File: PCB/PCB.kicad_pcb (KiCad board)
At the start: 2 copper layers, 121.6 x 80 mm, 113 parts, among them J1 AudioJack3, J2 Conn, J3 Screw_Terminal_01x02, J4 Screw_Terminal_01x02, J5 Screw_Terminal_01x02, J6 Screw_Terminal_01x02, Q1 Q_NPN_BCE, Q10 Q_NPN, Q11 Q_PNP_BCE, Q12 Q_NPN, Q13 Q_PNP, Q14 Q_PNP_BCE, Q15 Q_PNP_BCE, Q16 Q-NPN, Q17 Q-NPN, Q18 Q-NPN, Q19 Q-PNP, Q2 Q_PNP_BCE, Q20 Q-NPN, Q21 Q-PNP, Q22 Q-NPN, Q23 Q-PNP, Q24 Q-PNP, Q25 Q-NPN, Q26 Q-NPN, Q27 Q-PNP, Q28 Q-NPN, Q29 Q_PNP, Q3 Q_NPN_BCE, Q4 Q_PNP_BCE, Q5 Q_NPN_BCE, Q6 Q_PNP_BCE, Q7 Q_PNP_BCE, Q8 Q_NPN_BCE, Q9 Q_NPN_BCE

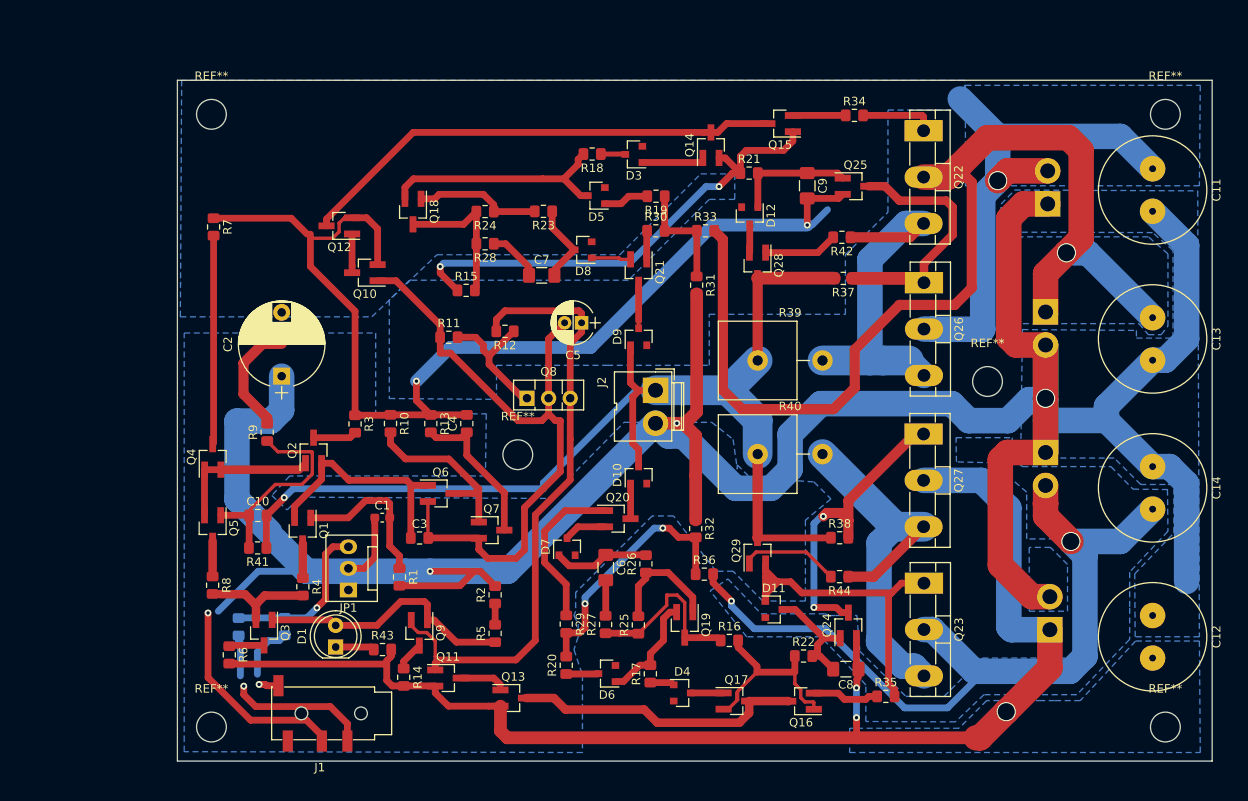
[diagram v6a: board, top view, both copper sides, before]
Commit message: Footprint actualizados. se agrando el pcb para los capacitores. Se agregaron algunos valores de componentes en el esquematico
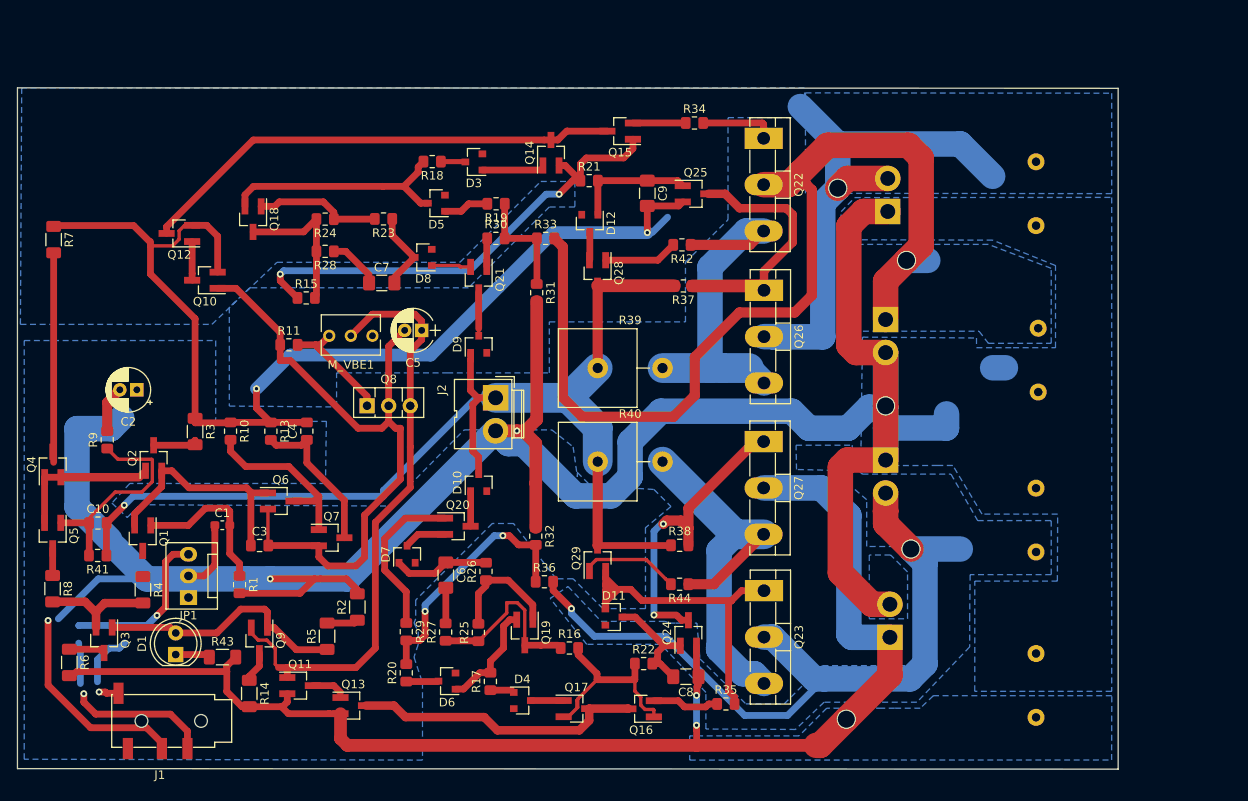
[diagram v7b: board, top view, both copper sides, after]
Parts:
- removed R12, R45, R46: R, Resistor_SMD:R_0805_2012Metric_Pad1.15x1.40mm_HandSolder
- removed REF** (x6): MountingHole_3.5mm, Mounting_Holes:MountingHole_3.5mm
- added M_VBE1: 5k, Potentiometer_THT:Potentiometer_Bourns_3266Y_Vertical, F.Cu at (174.2, 79.6)
- C11, C12, C13, C14: footprint Capacitor_THT:C_Radial_D12.5mm_H20.0mm_P5.00mm -> Capacitor_THT:C_Radial_D18.0mm_H35.5mm_P7.50mm; moved to B.Cu
- C2: value C -> 47u; footprint Capacitors_THT:CP_Radial_D10.0mm_P7.50mm -> Capacitor_THT:CP_Radial_D5.0mm_P2.00mm
- C3: value C -> 20p
- C4: value C -> 1u
- C5: value C -> 4.7u
- Q1, Q5, Q9: value Q_NPN_BCE -> MMBTA06
- Q2, Q4, Q6, Q7: value Q_PNP_BCE -> MMBTA56
- Q8: value Q_NPN_BCE -> MJE340
- R1: value R -> 20k
- R10: value R -> 1k
- R11: value R -> 2.2k
- R13: value R -> 10
- R14: value R -> 470; footprint Resistor_SMD:R_0805_2012Metric_Pad1.15x1.40mm_HandSolder -> Resistor_SMD:R_1206_3216Metric_Pad1.30x1.75mm_HandSolder
- R2, R5: value R -> 4.7k; footprint Resistor_SMD:R_0805_2012Metric_Pad1.15x1.40mm_HandSolder -> Resistor_SMD:R_1206_3216Metric_Pad1.30x1.75mm_HandSolder
- R3, R4, R7, R8: value R -> 22; footprint Resistor_SMD:R_0805_2012Metric_Pad1.15x1.40mm_HandSolder -> Resistor_SMD:R_1206_3216Metric_Pad1.30x1.75mm_HandSolder
- R43: value R -> TBD; footprint Resistor_SMD:R_0805_2012Metric_Pad1.15x1.40mm_HandSolder -> Resistor_SMD:R_1206_3216Metric_Pad1.30x1.75mm_HandSolder
- R6: value R -> 2.2k; footprint Resistor_SMD:R_0805_2012Metric_Pad1.15x1.40mm_HandSolder -> Resistor_SMD:R_1206_3216Metric_Pad1.30x1.75mm_HandSolder
- R9: value R -> 1.2k
- moved R5 19.7 mm to (174.0, 114.9)
- moved R7 18.9 mm to (141.9, 68.3)
- moved C6 18.8 mm to (187.9, 107.8)
- moved D11 18.8 mm to (207.7, 112.7)
- moved D8 18.8 mm to (185.3, 70.4)
- moved J2 18.8 mm to (193.8, 86.9)
- moved J3 18.8 mm to (239.9, 65.0)
- moved Q10 18.8 mm to (159.6, 73.1)
- moved Q12 18.8 mm to (156.6, 67.6)
- moved Q17 18.8 mm to (203.3, 123.4)
- moved Q18 18.8 mm to (165.3, 65.9)
- moved Q19 18.8 mm to (197.2, 114.5)
- moved Q20 18.8 mm to (189.4, 102.0)
- moved Q22 18.8 mm to (225.3, 56.4)
- moved Q23 18.8 mm to (225.3, 109.6)
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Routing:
- net GND: track 356.2 -> 303.2 mm
- net +15V: track 129.1 -> 118.3 mm
- net Net-(C2-Pad2): track 13.7 -> 5.47 mm
- net -15V: track 95.9 -> 90.6 mm
- net Net-(J1-PadS) (its old number): track 4.83 -> 0.00 mm
- net Net-(J1-PadS): track 19.5 -> 24.3 mm
- net Net-(Q1-Pad3): track 4.09 -> 0.04 mm
- net Net-(C5-Pad1): track 73.7 -> 71.1 mm
- net VEE: track 155.4 -> 157.4 mm
- net Net-(Q11-Pad3): track 5.60 -> 4.19 mm
- net Net-(R2-Pad1): track 2.48 -> 3.69 mm
- net Net-(Q5-Pad3): track 4.19 -> 3.19 mm
- net Net-(D1-Pad2): track 30.7 -> 29.8 mm
- net Net-(M_VBE1-Pad1): track 16.2 -> 15.6 mm
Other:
- board size 121.6 x 80 mm -> 129.3 x 80.1 mm

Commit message: More footprint changes. Added some modifications to the pcb
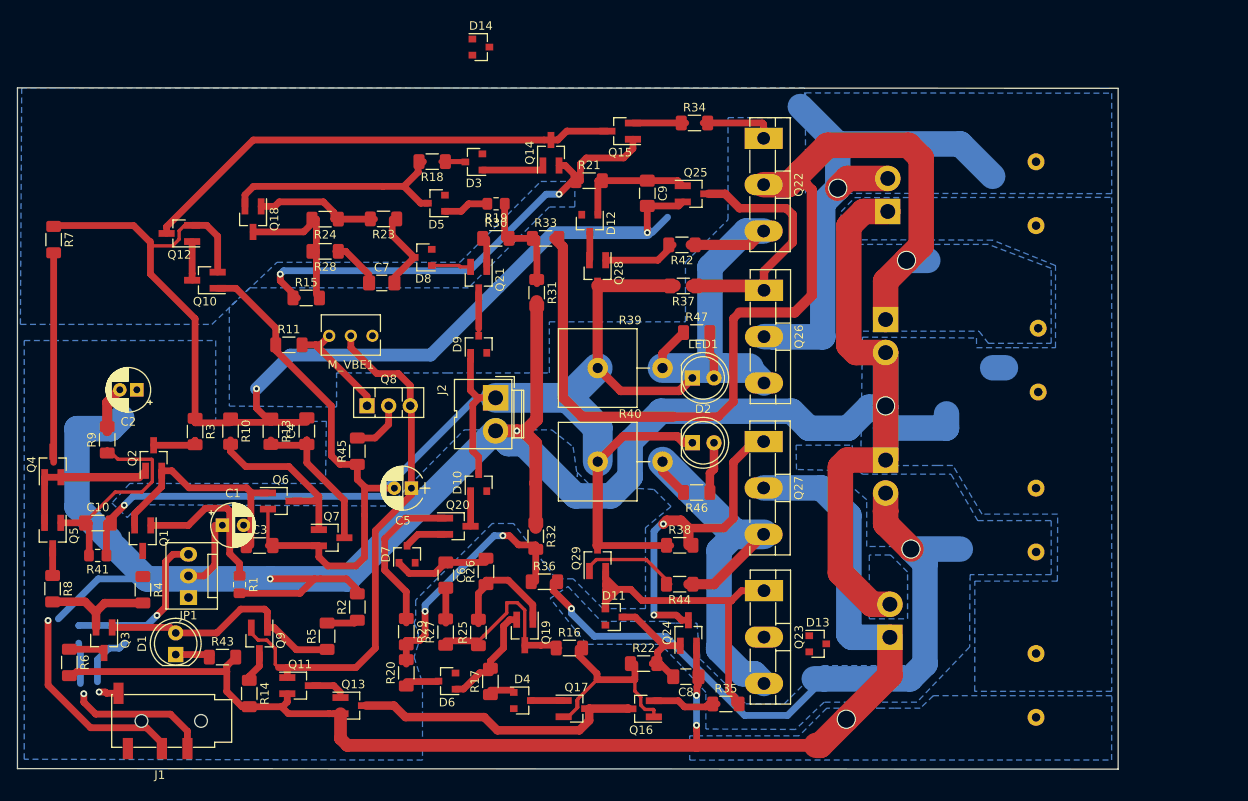
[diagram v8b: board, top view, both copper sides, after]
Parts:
- added D13: BAT54, Diode_SMD:D_SOT-23_ANK, F.Cu at (231.6, 115.8)
- added D14: BAT54, Diode_SMD:D_SOT-23_ANK, F.Cu at (192.1, 45.7)
- added D2: LED, LED_THT:LED_D5.0mm, F.Cu at (216.9, 92.2)
- added LED1: LED_ALT, LED_THT:LED_D5.0mm, F.Cu at (216.9, 84.6)
- added R45: 22, Resistor_SMD:R_1206_3216Metric_Pad1.30x1.75mm_HandSolder, F.Cu at (177.5, 93.2)
- added R46: TBD, Resistor_SMD:R_1206_3216Metric_Pad1.30x1.75mm_HandSolder, F.Cu at (217.4, 98.0)
- added R47: TBD, Resistor_SMD:R_1206_3216Metric_Pad1.30x1.75mm_HandSolder, F.Cu at (217.4, 79.2)
- C1: footprint Capacitor_SMD:C_0603_1608Metric_Pad1.05x0.95mm_HandSolder -> Capacitor_THT:CP_Radial_D5.0mm_P2.50mm
- C10: value C -> 4.7p; footprint Capacitor_SMD:C_0805_2012Metric_Pad1.15x1.40mm_HandSolder -> Capacitor_SMD:C_1206_3216Metric_Pad1.33x1.80mm_HandSolder
- C3, C4: footprint Capacitor_SMD:C_0805_2012Metric_Pad1.15x1.40mm_HandSolder -> Capacitor_SMD:C_1206_3216Metric_Pad1.33x1.80mm_HandSolder
- C6, C7: value C -> 5p
- C8, C9: value C -> 330p
- D10, D12, D3, D4, D5, D6, D7, D8, D9: value D_Sch -> BAT54
- Q10, Q12: value Q_NPN -> MMBTA06
- Q11, Q14, Q15: value Q_PNP_BCE -> MMBTA56
- Q13, Q29: value Q_PNP -> MMBTA56
- Q16, Q17, Q18, Q20, Q28: value Q-NPN -> MMBTA06
- Q19, Q21: value Q-PNP -> MMBTA56
- Q23, Q27: value Q-PNP -> 2SA1943
- Q24: value Q-PNP -> MJE350
- Q25: value Q-NPN -> MJE340
- Q26: value Q-NPN -> 2SC5200
- R10, R11, R13, R38, R9: footprint Resistor_SMD:R_0805_2012Metric_Pad1.15x1.40mm_HandSolder -> Resistor_SMD:R_1206_3216Metric_Pad1.30x1.75mm_HandSolder
- R15, R16, R31, R32: value R -> 47k; footprint Resistor_SMD:R_0805_2012Metric_Pad1.15x1.40mm_HandSolder -> Resistor_SMD:R_1206_3216Metric_Pad1.30x1.75mm_HandSolder
- R17, R18, R30: value R -> 100k; footprint Resistor_SMD:R_0805_2012Metric_Pad1.15x1.40mm_HandSolder -> Resistor_SMD:R_1206_3216Metric_Pad1.30x1.75mm_HandSolder
- R19: value R -> 80k
- R20: value R -> 80k; footprint Resistor_SMD:R_0805_2012Metric_Pad1.15x1.40mm_HandSolder -> Resistor_SMD:R_1206_3216Metric_Pad1.30x1.75mm_HandSolder
- R21, R22: value R -> 200; footprint Resistor_SMD:R_0805_2012Metric_Pad1.15x1.40mm_HandSolder -> Resistor_SMD:R_1206_3216Metric_Pad1.30x1.75mm_HandSolder
- R23, R26: value R -> 5k; footprint Resistor_SMD:R_0805_2012Metric_Pad1.15x1.40mm_HandSolder -> Resistor_SMD:R_1206_3216Metric_Pad1.30x1.75mm_HandSolder
- R24, R25, R37: value R -> 1k; footprint Resistor_SMD:R_0805_2012Metric_Pad1.15x1.40mm_HandSolder -> Resistor_SMD:R_1206_3216Metric_Pad1.30x1.75mm_HandSolder
- R27, R28: value R -> TBD; footprint Resistor_SMD:R_0805_2012Metric_Pad1.15x1.40mm_HandSolder -> Resistor_SMD:R_1206_3216Metric_Pad1.30x1.75mm_HandSolder
- R29: value R -> 75k; footprint Resistor_SMD:R_0805_2012Metric_Pad1.15x1.40mm_HandSolder -> Resistor_SMD:R_1206_3216Metric_Pad1.30x1.75mm_HandSolder
- R33, R36: value R -> 10k; footprint Resistor_SMD:R_0805_2012Metric_Pad1.15x1.40mm_HandSolder -> Resistor_SMD:R_1206_3216Metric_Pad1.30x1.75mm_HandSolder
- R34, R35: value R -> 4.7; footprint Resistor_SMD:R_0805_2012Metric_Pad1.15x1.40mm_HandSolder -> Resistor_SMD:R_1206_3216Metric_Pad1.30x1.75mm_HandSolder
- R39, R40: value R -> 0.1
- R42: value R -> 100; footprint Resistor_SMD:R_0805_2012Metric_Pad1.15x1.40mm_HandSolder -> Resistor_SMD:R_1206_3216Metric_Pad1.30x1.75mm_HandSolder
- R44: value R -> 25; footprint Resistor_SMD:R_0805_2012Metric_Pad1.15x1.40mm_HandSolder -> Resistor_SMD:R_1206_3216Metric_Pad1.30x1.75mm_HandSolder
- moved C5 18.6 mm to (183.9, 97.5)
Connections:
- Q18 pad 3: Net-(Q18-Pad3) -> VEE
- Q19 pad 3: Net-(Q19-Pad3) -> VCC
- Q22 pad 2: +15V -> Net-(D14-Pad1)
- Q23 pad 1: Net-(D11-Pad2) -> Net-(Q23-Pad1)
- Q23 pad 2: -15V -> Net-(D13-Pad2)
- Q8 pad 2: Net-(C3-Pad2) -> Net-(Q8-Pad2)
- R15 pad 2: Net-(Q18-Pad3) -> VEE
- R16 pad 1: Net-(Q19-Pad3) -> VCC
- R24 pad 2: Net-(Q18-Pad3) -> VEE
- R25 pad 1: Net-(Q19-Pad3) -> VCC
- R27 pad 1: Net-(Q19-Pad3) -> VCC
- R28 pad 2: Net-(Q18-Pad3) -> VEE
- R35 pad 2: Net-(D11-Pad2) -> Net-(Q23-Pad1)
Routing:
- net Net-(C10-Pad2): track 136.7 -> 162.2 mm
- net VCC: track 195.2 -> 216.0 mm
- net Net-(Q19-Pad3): track 20.7 -> 0.00 mm
- net Net-(Q18-Pad3): track 17.6 -> 0.00 mm
- net VEE: track 157.4 -> 175.0 mm
- net Net-(C3-Pad2): track 77.3 -> 62.6 mm
- net -15V: track 90.6 -> 82.6 mm
- net Net-(C5-Pad1): track 71.1 -> 63.5 mm
- net Net-(Q8-Pad2): track 0.00 -> 6.53 mm
- net Net-(D2-Pad2): track 0.00 -> 6.04 mm
- net Net-(LED1-Pad2): track 0.00 -> 5.53 mm
- net Net-(Q22-Pad3): track 44.4 -> 49.6 mm
- net Net-(Q23-Pad3): track 51.5 -> 56.2 mm
- net Net-(Q24-Pad3): track 35.5 -> 39.0 mm
- net +15V: track 118.3 -> 121.4 mm
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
